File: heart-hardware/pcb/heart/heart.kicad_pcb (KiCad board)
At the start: 2 copper layers, 61.3 x 56.1 mm, 49 parts, among them J1 3V0, J2 DIO, J3 CLK, J4 GND, SW1 SW_SPDT, U1 STM32L031F6Px, U2 TCA6416APWR, U3 LIS3DH

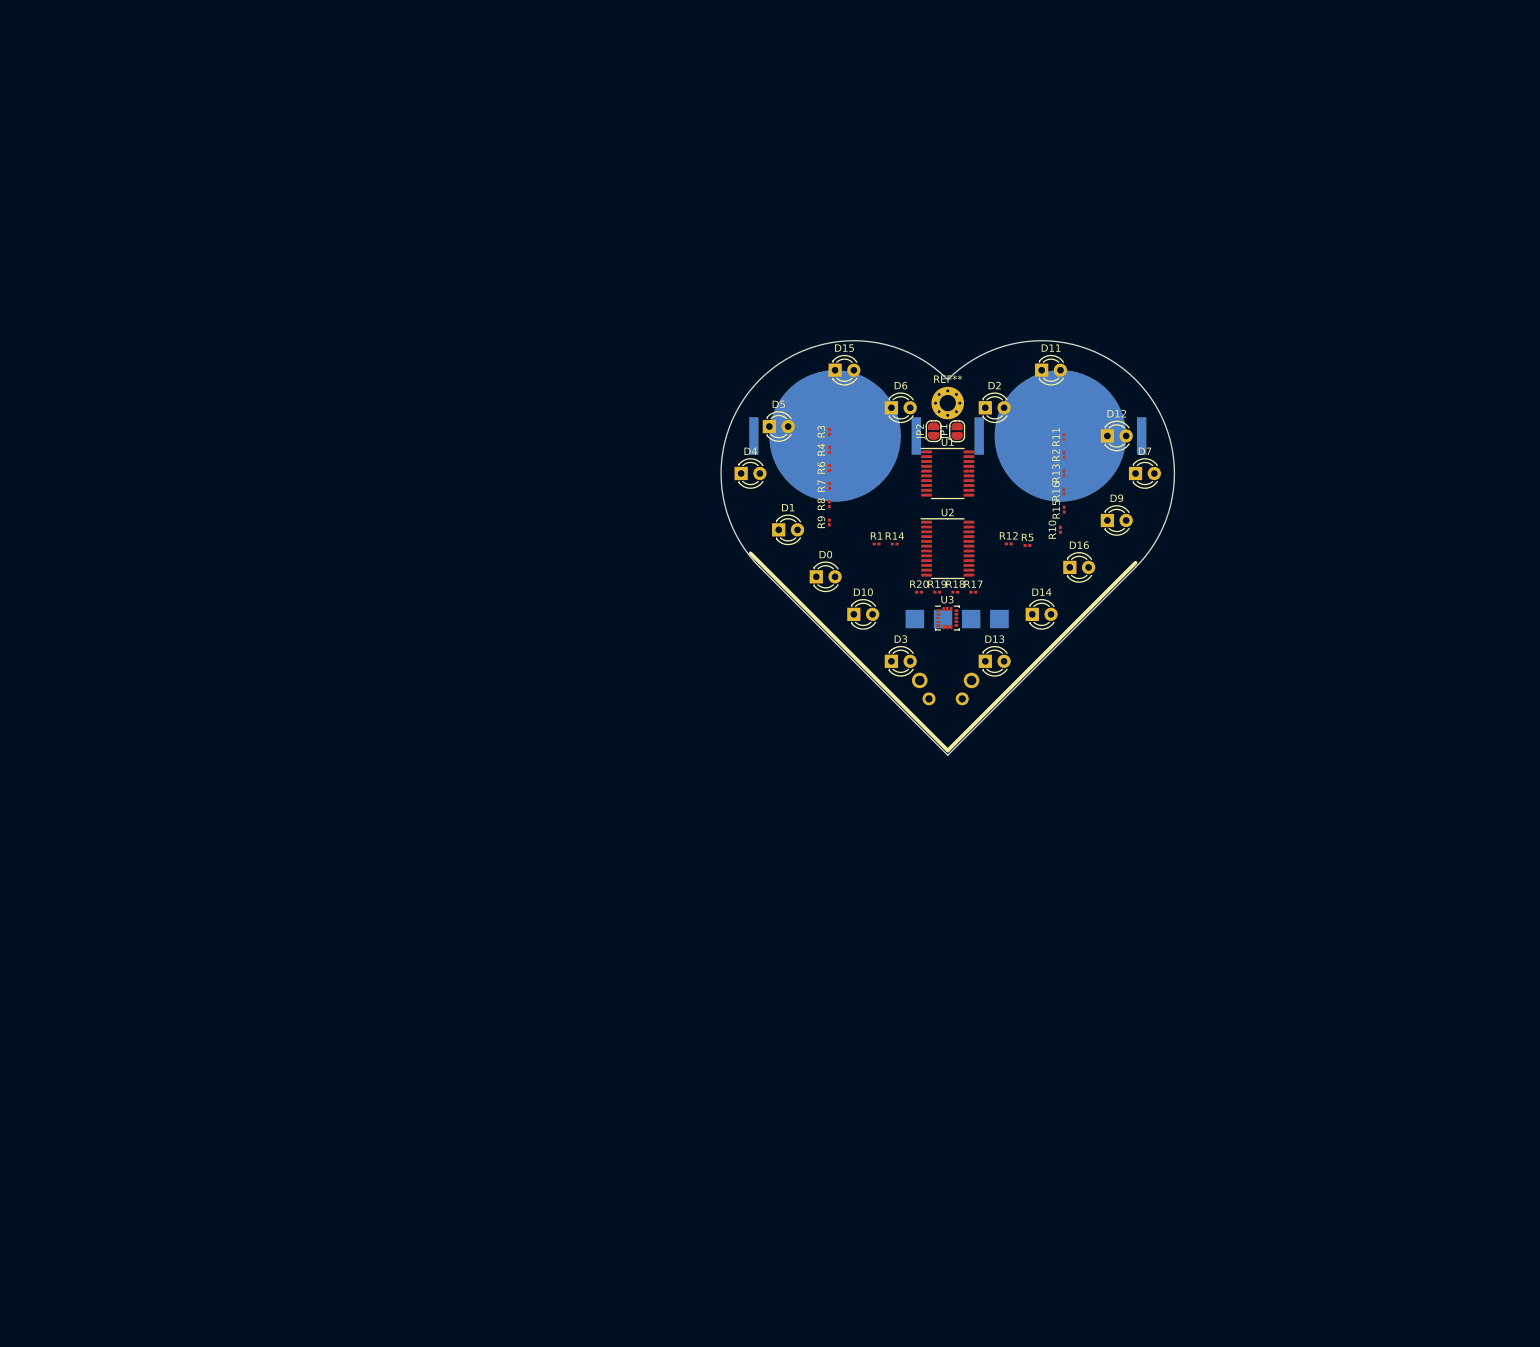
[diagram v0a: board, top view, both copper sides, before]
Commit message: Schematic complete (ver. 1.0), starting work on a pcb and choose footprints
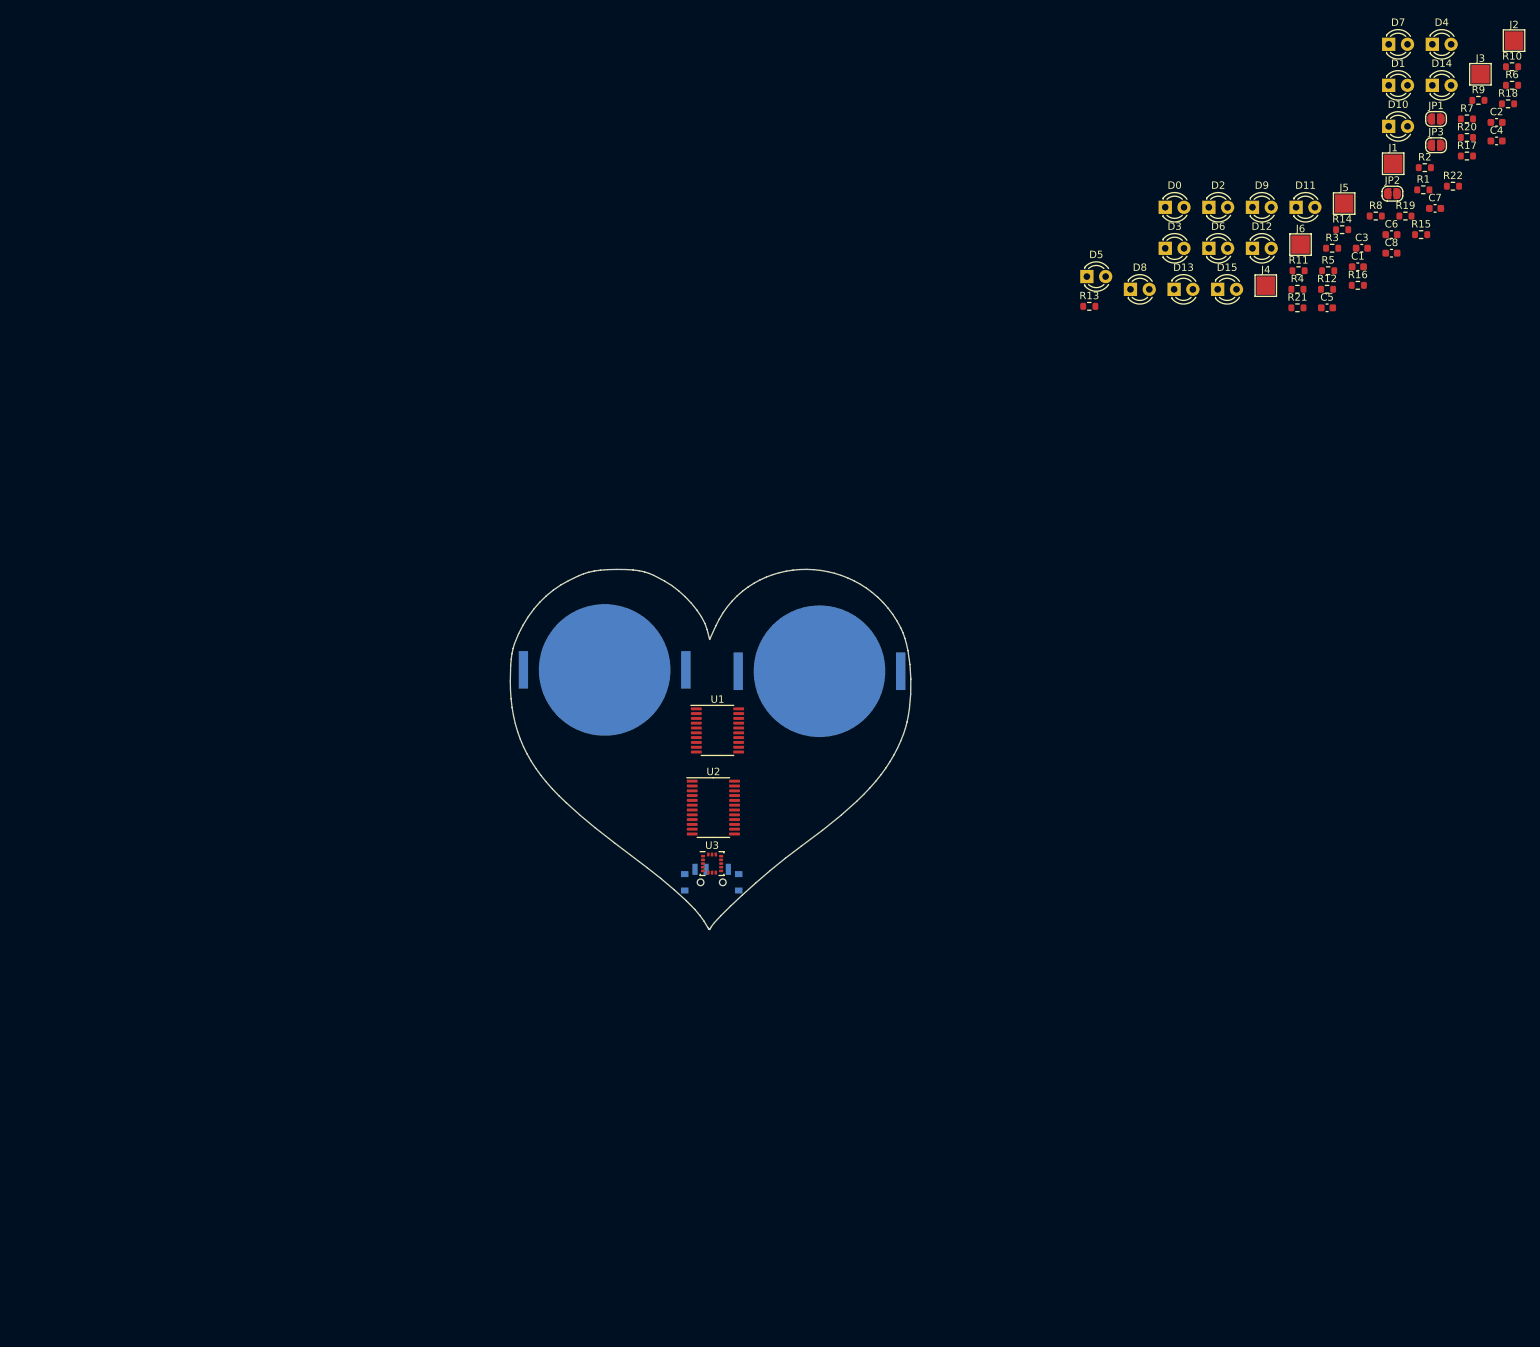
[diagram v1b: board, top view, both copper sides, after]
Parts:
- removed D16: LED, LED_THT:LED_D3.0mm
- removed REF**: MountingHole_2.2mm_M2_Pad_Via, MountingHole:MountingHole_2.2mm_M2_Pad_Via
- added C1: 10nF, Capacitor_SMD:C_0603_1608Metric, F.Cu at (207.9, 22.8)
- added C2: 100nF, Capacitor_SMD:C_0603_1608Metric, F.Cu at (226.6, 3.31)
- added C3: 10nF, Capacitor_SMD:C_0603_1608Metric, F.Cu at (208.4, 20.3)
- added C4: 100nF, Capacitor_SMD:C_0603_1608Metric, F.Cu at (226.6, 5.82)
- added C5: 100nF, Capacitor_SMD:C_0603_1608Metric, F.Cu at (203.7, 28.4)
- added C6: 10nF, Capacitor_SMD:C_0603_1608Metric, F.Cu at (212.4, 18.5)
- added C7: 10uF, Capacitor_SMD:C_0603_1608Metric, F.Cu at (218.3, 14.9)
- added C8: 100nF, Capacitor_SMD:C_0603_1608Metric, F.Cu at (212.4, 21.0)
- added D8: LED, LED_THT:LED_D3.0mm, F.Cu at (177.1, 25.9)
- added J5: PROB1, TestPoint:TestPoint_Pad_2.5x2.5mm, F.Cu at (206.0, 14.3)
- added J6: PROB2, TestPoint:TestPoint_Pad_2.5x2.5mm, F.Cu at (200.1, 19.8)
- added JP3: Jumper, Jumper:SolderJumper-2_P1.3mm_Open_RoundedPad1.0x1.5mm, F.Cu at (218.4, 6.40)
- added R21: 10k, Resistor_SMD:R_0603_1608Metric, F.Cu at (199.7, 28.4)
- added R22: 10k, Resistor_SMD:R_0603_1608Metric, F.Cu at (220.7, 11.9)
- J1, J2, J3, J4: moved to F.Cu
- R1: value R -> 10k; footprint Capacitor_SMD:C_0201_0603Metric -> Resistor_SMD:R_0603_1608Metric
- R10, R11, R12, R13, R14, R15, R16, R17, R18, R19, R2, R20, R3, R5, R6, R7, R8, R9: footprint Capacitor_SMD:C_0201_0603Metric -> Resistor_SMD:R_0603_1608Metric
- R4: value R -> R_Small; footprint Capacitor_SMD:C_0201_0603Metric -> Resistor_SMD:R_0603_1608Metric
- SW1: footprint Button_Switch_THT:SW_Tactile_SPST_Angled_PTS645Vx39-2LFS -> Button_Switch_SMD:SW_SPDT_PCM12
- moved D4 110.0 mm to (217.9, -7.25)
- moved J2 109.9 mm to (229.0, -7.75)
- moved R6 105.9 mm to (228.7, -1.71), turned to 0 degrees
- moved R9 104.7 mm to (224.2, 0.33), turned to 0 degrees
- moved D1 102.1 mm to (212.0, -1.70)
- moved J3 100.9 mm to (224.4, -3.20)
- moved R18 99.8 mm to (228.2, 0.80)
- moved R7 99.5 mm to (222.6, 2.84), turned to 0 degrees
- moved D10 97.9 mm to (212.0, 3.85)
- moved R20 96.3 mm to (222.6, 5.35)
- moved D14 89.7 mm to (217.9, -1.70)
- moved R17 89.1 mm to (222.6, 7.86)
- moved R1 88.1 mm to (216.7, 12.4)
- moved R10 87.5 mm to (228.7, -4.22), turned to 0 degrees
- moved R8 83.6 mm to (210.3, 16.0), turned to 0 degrees
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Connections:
- net Net-(R4-Pad1) renamed TCA6416A_RESET
- R1 pad 1: Net-(R1-Pad1) -> GND
- R10 pad 1: Net-(R10-Pad1) -> Net-(D5-Pad2)
- R10 pad 2: Net-(R10-Pad2) -> +3V0
- R11 pad 1: Net-(R11-Pad1) -> Net-(D6-Pad2)
- R11 pad 2: Net-(R11-Pad2) -> +3V0
- R12 pad 1: Net-(R12-Pad1) -> Net-(D7-Pad2)
- R12 pad 2: Net-(R12-Pad2) -> +3V0
- R13 pad 2: Net-(R13-Pad2) -> +3V0
- R14 pad 1: Net-(R14-Pad1) -> Net-(D9-Pad2)
- R14 pad 2: Net-(R14-Pad2) -> +3V0
- R15 pad 1: Net-(R15-Pad1) -> Net-(D10-Pad2)
- R15 pad 2: Net-(R15-Pad2) -> +3V0
- R16 pad 1: Net-(R16-Pad1) -> Net-(D11-Pad2)
- R16 pad 2: Net-(R16-Pad2) -> +3V0
- R2 pad 1: Net-(R2-Pad1) -> I2C_SCL
- R2 pad 2: Net-(R2-Pad2) -> +3V0
- R3 pad 1: Net-(R3-Pad1) -> +3V0
- R3 pad 2: Net-(R3-Pad2) -> I2C_SDA
- R4 pad 2: Net-(R4-Pad2) -> +3V0
- R5 pad 1: Net-(R5-Pad1) -> Net-(D2-Pad2)
- R5 pad 2: Net-(R5-Pad2) -> +3V0
- R6 pad 1: Net-(R6-Pad1) -> Net-(D3-Pad2)
- R6 pad 2: Net-(R6-Pad2) -> +3V0
- R9 pad 1: Net-(R9-Pad1) -> Net-(D4-Pad2)
- R9 pad 2: Net-(R9-Pad2) -> +3V0
- U1 pad 12: LIS3DH_INT1 -> Net-(JP3-Pad1)
- U1 pad 13: LIS3DH_INT2 -> Net-(U1-Pad13)
- U1 pad 6: Net-(U1-Pad6) -> LIS3DH_INT1
- U1 pad 8: Net-(U1-Pad8) -> LIS3DH_INT2
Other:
- board size 61.3 x 56.1 mm -> 54.2 x 48.7 mm

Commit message: PCB design update
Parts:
- removed BT1, BT2: CR2032, Battery:BatteryHolder_Keystone_3034_1x20mm
- removed J5: PROB1, TestPoint:TestPoint_Pad_2.5x2.5mm
- removed J6: PROB2, TestPoint:TestPoint_Pad_2.5x2.5mm
- removed JP1: Jumper, Jumper:SolderJumper-2_P1.3mm_Open_RoundedPad1.0x1.5mm
- removed JP2: Current Probe, Jumper:SolderJumper-2_P1.3mm_Open_RoundedPad1.0x1.5mm
- added  : , MountingHole:MountingHole_2.5mm_Pad_Via, F.Cu at (157.4, 118.4)
- added  : AMP, Jumper:SolderJumper-2_P1.3mm_Open_RoundedPad1.0x1.5mm, B.Cu at (157.9, 144.6)
- added  : PWR, Jumper:SolderJumper-2_P1.3mm_Open_RoundedPad1.0x1.5mm, B.Cu at (155.3, 141.8)
- added  : CR2032, Battery:BatteryHolder_Keystone_3034_1x20mm, B.Cu at (145.9, 127.0)
- added  : CR2032, Battery:BatteryHolder_Keystone_3034_1x20mm, B.Cu at (168.8, 127.0)
- added C0: 47uF, Capacitor_SMD:C_1210_3225Metric_Pad1.33x2.70mm_HandSolder, F.Cu at (170.7, 35.3)
- added C9: 100nF, Capacitor_SMD:C_0402_1005Metric, F.Cu at (187.7, 28.4)
- C1: value 10nF -> 100nF
- C2, C3, C4: footprint Capacitor_SMD:C_0603_1608Metric -> Capacitor_SMD:C_0402_1005Metric
- C5: value 100nF -> 10nF; footprint Capacitor_SMD:C_0603_1608Metric -> Capacitor_SMD:C_0402_1005Metric
- C6: value 10nF -> 100nF; footprint Capacitor_SMD:C_0603_1608Metric -> Capacitor_SMD:C_0402_1005Metric
- C7: value 10uF -> 10nF; footprint Capacitor_SMD:C_0603_1608Metric -> Capacitor_SMD:C_0402_1005Metric
- C8: value 100nF -> 10uF; footprint Capacitor_SMD:C_0603_1608Metric -> Capacitor_SMD:C_0402_1005Metric
- D0, D1, D10, D11, D12, D13, D14, D15, D2, D3, D4, D5, D6, D7, D8, D9: footprint LED_THT:LED_D3.0mm -> LED_SMD:LED_0603_1608Metric
- J1, J2, J3, J4: footprint TestPoint:TestPoint_Pad_2.5x2.5mm -> TestPoint:TestPoint_Pad_1.0x1.0mm
- R1, R10, R11, R12, R13, R14, R15, R16, R17, R18, R19, R20, R21, R22, R4, R5, R6, R7, R8, R9: footprint Resistor_SMD:R_0603_1608Metric -> Resistor_SMD:R_0402_1005Metric
- R2, R3: value R -> 10k; footprint Resistor_SMD:R_0603_1608Metric -> Resistor_SMD:R_0402_1005Metric
- SW1: value SW_SPDT -> (none)
- moved D14 195.3 mm to (89.1, 145.1)
- moved D10 185.8 mm to (81.1, 135.7)
- moved D11 170.2 mm to (95.0, 149.2)
- moved D7 162.9 mm to (109.5, 119.3)
- moved D4 161.1 mm to (115.9, 117.4)
- moved D1 156.9 mm to (124.1, 128.2)
- moved D0 153.1 mm to (108.6, 149.2)
- moved D2 150.9 mm to (112.5, 145.6)
- moved D15 149.6 mm to (79.6, 128.1)
- moved D8 147.0 mm to (84.6, 140.1)
- moved D12 142.2 mm to (118.1, 140.8)
- moved D3 142.1 mm to (82.4, 121.9)
- moved D9 141.1 mm to (122.1, 136.5)
- moved D6 138.3 mm to (89.9, 118.2)
- moved D5 120.5 mm to (97.2, 119.2)
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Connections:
- C1 pad 1: Net-(C1-Pad1) -> +3V0
- C5 pad 1: +3V0 -> Net-(C5-Pad1)
- C6 pad 1: GND -> +3V0
- C6 pad 2: +3V0 -> GND
- C8 pad 1: +3V0 -> GND
- C8 pad 2: GND -> +3V0
- U1 pad 4: Net-(C1-Pad1) -> Net-(C5-Pad1)
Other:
- board size 54.2 x 48.7 mm -> 49.5 x 44 mm
- copper layers 2 -> 4
- board text added: "OFF"
- board text added: "ON"
